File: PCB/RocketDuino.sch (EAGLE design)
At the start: 42 parts, among them J1 FTDI, Y1 16MHZ

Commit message: New DRU settings
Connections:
- net RX2: now also SERIAL2.2; no longer SERIAL2.3
- net TX2: now also SERIAL2.3; no longer SERIAL2.2
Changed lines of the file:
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@@
 </segment>
 <segment>
-<pinref part="SERIAL2" gate="G$1" pin="2"/>
-<wire x1="256.54" y1="185.42" x2="264.16" y2="185.42" width="0.1524" layer="91"/>
-<label x="259.08" y="185.42" size="1.778" layer="95"/>
+<pinref part="SERIAL2" gate="G$1" pin="3"/>
+<wire x1="256.54" y1="187.96" x2="264.16" y2="187.96" width="0.1524" layer="91"/>
+<label x="259.08" y="187.96" size="1.778" layer="95"/>
 </segment>
 </net>
@@
 </segment>
 <segment>
-<pinref part="SERIAL2" gate="G$1" pin="3"/>
-<wire x1="256.54" y1="187.96" x2="264.16" y2="187.96" width="0.1524" layer="91"/>
-<label x="259.08" y="187.96" size="1.778" layer="95"/>
+<pinref part="SERIAL2" gate="G$1" pin="2"/>
+<wire x1="256.54" y1="185.42" x2="264.16" y2="185.42" width="0.1524" layer="91"/>
+<label x="259.08" y="185.42" size="1.778" layer="95"/>
 </segment>
 </net>

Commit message: Cleanups from Reddit post
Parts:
- added C11, C12: 0.1uF, SparkFun-Capacitors:CAP1206
- R1, R3: value 100Ω -> 150Ω
- R2, R4: value 150Ω -> 220Ω
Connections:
- net 5V: now also C11.1, C12.1
- net GND: now also C11.2, C12.2
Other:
- note added: "0.8"
- note removed: "0.4"
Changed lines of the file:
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@@
 <part name="C8" library="SparkFun-Capacitors" deviceset="CAP" device="1206" value="0.1uF"/>
 <part name="C9" library="SparkFun-Capacitors" deviceset="CAP" device="1206" value="0.22uF"/>
-<part name="R4" library="SparkFun-Resistors" deviceset="RESISTOR" device="1206" value="150Ω"/>
+<part name="R4" library="SparkFun-Resistors" deviceset="RESISTOR" device="1206" value="220Ω"/>
 <part name="R10" library="SparkFun-Resistors" deviceset="RESISTOR" device="1206" value="10KΩ"/>
 <part name="GND7" library="SparkFun-Aesthetics" deviceset="GND" device=""/>
@@
 <part name="GND13" library="SparkFun-Aesthetics" deviceset="GND" device=""/>
 <part name="POWER" library="led" deviceset="LED" device="SML0805"/>
-<part name="R1" library="SparkFun-Resistors" deviceset="RESISTOR" device="1206" value="100Ω"/>
+<part name="R1" library="SparkFun-Resistors" deviceset="RESISTOR" device="1206" value="150Ω"/>
 <part name="GPS" library="led" deviceset="LED" device="SML0805"/>
-<part name="R3" library="SparkFun-Resistors" deviceset="RESISTOR" device="1206" value="100Ω"/>
+<part name="R3" library="SparkFun-Resistors" deviceset="RESISTOR" device="1206" value="150Ω"/>
 <part name="RX" library="led" deviceset="LED" device="SML0805"/>
-<part name="R2" library="SparkFun-Resistors" deviceset="RESISTOR" device="1206" value="150Ω"/>
+<part name="R2" library="SparkFun-Resistors" deviceset="RESISTOR" device="1206" value="220Ω"/>
 <part name="MOS1" library="SparkFun-DiscreteSemi" deviceset="MOSFET-NCHANNEL" device="FQP30N06L" value=""/>
 <part name="MOS2" library="SparkFun-DiscreteSemi" deviceset="MOSFET-NCHANNEL" device="FQP30N06L" value=""/>
@@
 <part name="SERIAL2" library="SparkFun-Connectors" deviceset="M04" device="POLAR"/>
 <part name="SUPPLY6" library="SparkFun-Aesthetics" deviceset="5V" device=""/>
+<part name="C11" library="SparkFun-Capacitors" deviceset="CAP" device="1206" value="0.1uF"/>
+<part name="C12" library="SparkFun-Capacitors" deviceset="CAP" device="1206" value="0.1uF"/>
 </parts>
 <sheets>
@@
 <text x="147.32" y="40.64" size="1.778" layer="97">red</text>
 <text x="231.14" y="2.54" size="5.08" layer="97">Joshua Villwock</text>
-<text x="299.974" y="1.27" size="3.81" layer="97">0.4</text>
+<text x="299.974" y="1.27" size="3.81" layer="97">0.8</text>
 <wire x1="-5.08" y1="266.7" x2="312.42" y2="266.7" width="0.1524" layer="94"/>
 <wire x1="312.42" y1="266.7" x2="312.42" y2="-5.08" width="0.1524" layer="94"/>
@@
 <instance part="SERIAL2" gate="G$1" x="251.46" y="185.42"/>
 <instance part="SUPPLY6" gate="G$1" x="259.08" y="190.5"/>
+<instance part="C11" gate="G$1" x="48.26" y="180.34"/>
+<instance part="C12" gate="G$1" x="38.1" y="180.34"/>
 </instances>
 <busses>
@@
 <wire x1="58.42" y1="177.8" x2="58.42" y2="172.72" width="0.1524" layer="91"/>
 <wire x1="58.42" y1="172.72" x2="71.12" y2="172.72" width="0.1524" layer="91"/>
+<pinref part="C12" gate="G$1" pin="2"/>
+<wire x1="58.42" y1="172.72" x2="48.26" y2="172.72" width="0.1524" layer="91"/>
+<wire x1="48.26" y1="172.72" x2="38.1" y2="172.72" width="0.1524" layer="91"/>
+<wire x1="38.1" y1="172.72" x2="38.1" y2="177.8" width="0.1524" layer="91"/>
+<junction x="58.42" y="172.72"/>
+<pinref part="C11" gate="G$1" pin="2"/>
+<wire x1="48.26" y1="177.8" x2="48.26" y2="172.72" width="0.1524" layer="91"/>
+<junction x="48.26" y="172.72"/>
 </segment>
 <segment>
@@
 <wire x1="58.42" y1="185.42" x2="58.42" y2="190.5" width="0.1524" layer="91"/>
 <wire x1="58.42" y1="190.5" x2="68.58" y2="190.5" width="0.1524" layer="91"/>
+<pinref part="C12" gate="G$1" pin="1"/>
+<wire x1="58.42" y1="190.5" x2="48.26" y2="190.5" width="0.1524" layer="91"/>
+<wire x1="48.26" y1="190.5" x2="38.1" y2="190.5" width="0.1524" layer="91"/>
+<wire x1="38.1" y1="190.5" x2="38.1" y2="185.42" width="0.1524" layer="91"/>
+<junction x="58.42" y="190.5"/>
+<pinref part="C11" gate="G$1" pin="1"/>
+<wire x1="48.26" y1="185.42" x2="48.26" y2="190.5" width="0.1524" layer="91"/>
+<junction x="48.26" y="190.5"/>
 </segment>
 <segment>
@@
 </sheet>
 </sheets>
-<errors>
-</errors>
 </schematic>
 </drawing>

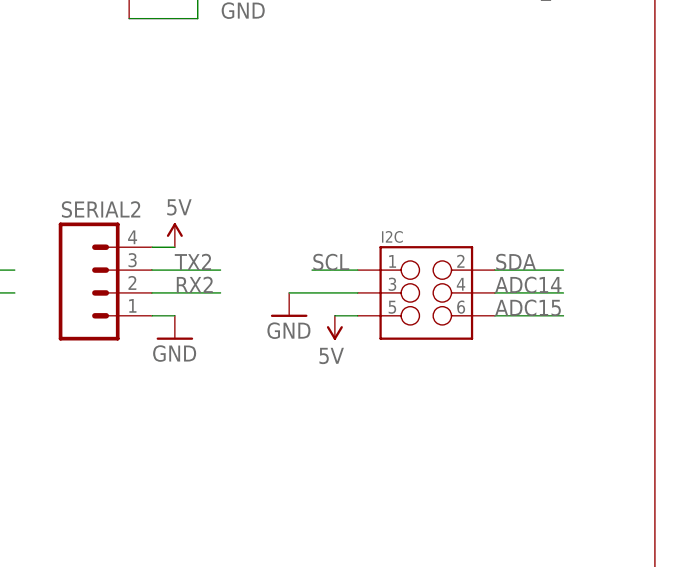
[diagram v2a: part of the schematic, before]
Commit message: Non-SMT I2C connector
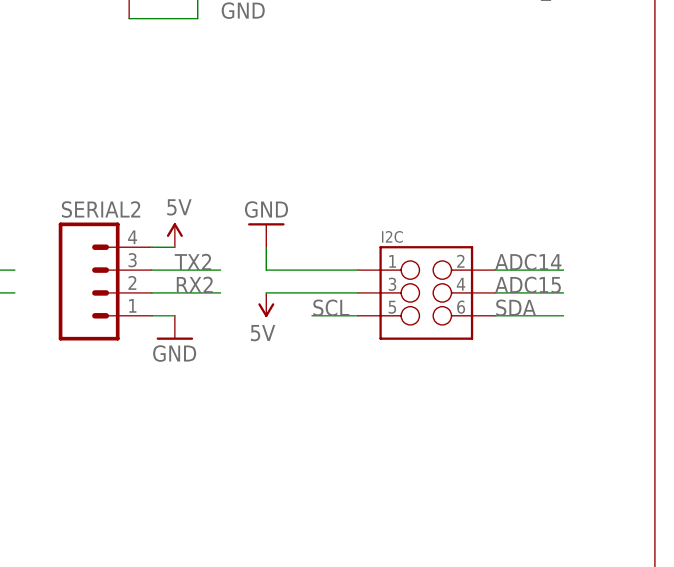
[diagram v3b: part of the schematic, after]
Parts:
- I2C: device SparkFun-Connectors:M03X2FEMALE_SMD -> SparkFun-Connectors:M03X2FEMALE
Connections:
- net 5V: now also I2C.3; no longer I2C.5
- net ADC14: now also I2C.2; no longer I2C.4
- net ADC15: now also I2C.4; no longer I2C.6
- net GND: now also I2C.1; no longer I2C.3
- net SCL: now also I2C.5; no longer I2C.1
- net SDA: now also I2C.6; no longer I2C.2
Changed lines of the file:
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@@
 <part name="GND8" library="SparkFun-Aesthetics" deviceset="GND" device=""/>
 <part name="SUPPLY4" library="SparkFun-Aesthetics" deviceset="5V" device=""/>
-<part name="I2C" library="SparkFun-Connectors" deviceset="M03X2" device="FEMALE_SMD"/>
-<part name="SUPPLY10" library="SparkFun-Aesthetics" deviceset="5V" device=""/>
-<part name="GND14" library="SparkFun-Aesthetics" deviceset="GND" device=""/>
+<part name="I2C" library="SparkFun-Connectors" deviceset="M03X2" device="FEMALE"/>
 <part name="FRAME1" library="SparkFun-Aesthetics" deviceset="FRAME-LEDGER" device=""/>
 <part name="GND15" library="SparkFun-Aesthetics" deviceset="GND" device=""/>
@@
 <part name="C11" library="SparkFun-Capacitors" deviceset="CAP" device="1206" value="0.1uF"/>
 <part name="C12" library="SparkFun-Capacitors" deviceset="CAP" device="1206" value="0.1uF"/>
+<part name="SUPPLY7" library="SparkFun-Aesthetics" deviceset="5V" device=""/>
+<part name="GND10" library="SparkFun-Aesthetics" deviceset="GND" device=""/>
 </parts>
 <sheets>
@@
 <instance part="SUPPLY4" gate="G$1" x="287.02" y="83.82"/>
 <instance part="I2C" gate="G$1" x="287.02" y="185.42"/>
-<instance part="SUPPLY10" gate="G$1" x="276.86" y="182.88" rot="R180"/>
-<instance part="GND14" gate="1" x="271.78" y="182.88"/>
 <instance part="FRAME1" gate="G$2" x="210.82" y="-5.08"/>
 <instance part="GND15" gate="1" x="289.56" y="251.46"/>
@@
 <instance part="C11" gate="G$1" x="48.26" y="180.34"/>
 <instance part="C12" gate="G$1" x="38.1" y="180.34"/>
+<instance part="SUPPLY7" gate="G$1" x="269.24" y="185.42" rot="R180"/>
+<instance part="GND10" gate="1" x="269.24" y="193.04" rot="R180"/>
 </instances>
 <busses>
@@
 </segment>
 <segment>
-<pinref part="GND14" gate="1" pin="GND"/>
-<pinref part="I2C" gate="G$1" pin="3"/>
-<wire x1="271.78" y1="185.42" x2="279.4" y2="185.42" width="0.1524" layer="91"/>
-</segment>
-<segment>
 <pinref part="MOS" gate="G$1" pin="2"/>
 <pinref part="GND15" gate="1" pin="GND"/>
@@
 <wire x1="228.6" y1="182.88" x2="231.14" y2="182.88" width="0.1524" layer="91"/>
 <pinref part="GND16" gate="1" pin="GND"/>
+</segment>
+<segment>
+<pinref part="GND10" gate="1" pin="GND"/>
+<wire x1="269.24" y1="190.5" x2="269.24" y2="187.96" width="0.1524" layer="91"/>
+<pinref part="I2C" gate="G$1" pin="1"/>
+<wire x1="269.24" y1="187.96" x2="279.4" y2="187.96" width="0.1524" layer="91"/>
 </segment>
 </net>
@@
 </segment>
 <segment>
-<pinref part="SUPPLY10" gate="G$1" pin="5V"/>
-<pinref part="I2C" gate="G$1" pin="5"/>
-<wire x1="276.86" y1="182.88" x2="279.4" y2="182.88" width="0.1524" layer="91"/>
-</segment>
-<segment>
 <pinref part="SERIAL1" gate="G$1" pin="4"/>
 <wire x1="228.6" y1="190.5" x2="231.14" y2="190.5" width="0.1524" layer="91"/>
@@
 <pinref part="SUPPLY6" gate="G$1" pin="5V"/>
 <wire x1="256.54" y1="190.5" x2="259.08" y2="190.5" width="0.1524" layer="91"/>
+</segment>
+<segment>
+<pinref part="SUPPLY7" gate="G$1" pin="5V"/>
+<pinref part="I2C" gate="G$1" pin="3"/>
+<wire x1="269.24" y1="185.42" x2="279.4" y2="185.42" width="0.1524" layer="91"/>
 </segment>
 </net>
@@
 </segment>
 <segment>
+<pinref part="I2C" gate="G$1" pin="6"/>
+<wire x1="294.64" y1="182.88" x2="302.26" y2="182.88" width="0.1524" layer="91"/>
+<label x="294.64" y="182.88" size="1.778" layer="95"/>
+</segment>
+</net>
+<net name="SCL" class="0">
+<segment>
+<pinref part="ATMEGA2560AU" gate="1" pin="(SCL/INT0)PD0"/>
+<wire x1="160.02" y1="132.08" x2="149.86" y2="132.08" width="0.1524" layer="91"/>
+<label x="152.4" y="132.08" size="1.778" layer="95"/>
+</segment>
+<segment>
+<pinref part="I2C" gate="G$1" pin="5"/>
+<wire x1="279.4" y1="182.88" x2="274.32" y2="182.88" width="0.1524" layer="91"/>
+<label x="274.32" y="182.88" size="1.778" layer="95"/>
+</segment>
+</net>
+<net name="ADC14" class="0">
+<segment>
+<pinref part="ATMEGA2560AU" gate="1" pin="PK6(ADC14/PCINT22)"/>
+<wire x1="78.74" y1="129.54" x2="68.58" y2="129.54" width="0.1524" layer="91"/>
+<label x="68.58" y="129.54" size="1.778" layer="95"/>
+</segment>
+<segment>
 <pinref part="I2C" gate="G$1" pin="2"/>
 <wire x1="294.64" y1="187.96" x2="302.26" y2="187.96" width="0.1524" layer="91"/>
@@
 </segment>
 </net>
-<net name="SCL" class="0">
-<segment>
-<pinref part="ATMEGA2560AU" gate="1" pin="(SCL/INT0)PD0"/>
-<wire x1="160.02" y1="132.08" x2="149.86" y2="132.08" width="0.1524" layer="91"/>
-<label x="152.4" y="132.08" size="1.778" layer="95"/>
-</segment>
-<segment>
-<pinref part="I2C" gate="G$1" pin="1"/>
-<wire x1="279.4" y1="187.96" x2="274.32" y2="187.96" width="0.1524" layer="91"/>
-<label x="274.32" y="187.96" size="1.778" layer="95"/>
-</segment>
-</net>
-<net name="ADC14" class="0">
-<segment>
-<pinref part="ATMEGA2560AU" gate="1" pin="PK6(ADC14/PCINT22)"/>
-<wire x1="78.74" y1="129.54" x2="68.58" y2="129.54" width="0.1524" layer="91"/>
-<label x="68.58" y="129.54" size="1.778" layer="95"/>
+<net name="ADC15" class="0">
+<segment>
+<pinref part="ATMEGA2560AU" gate="1" pin="PK7(ADC15/PCINT23)"/>
+<wire x1="78.74" y1="132.08" x2="68.58" y2="132.08" width="0.1524" layer="91"/>
+<label x="68.58" y="132.08" size="1.778" layer="95"/>
 </segment>
 <segment>
@@
 </segment>
 </net>
-<net name="ADC15" class="0">
-<segment>
-<pinref part="ATMEGA2560AU" gate="1" pin="PK7(ADC15/PCINT23)"/>
-<wire x1="78.74" y1="132.08" x2="68.58" y2="132.08" width="0.1524" layer="91"/>
-<label x="68.58" y="132.08" size="1.778" layer="95"/>
-</segment>
-<segment>
-<pinref part="I2C" gate="G$1" pin="6"/>
-<wire x1="294.64" y1="182.88" x2="302.26" y2="182.88" width="0.1524" layer="91"/>
-<label x="294.64" y="182.88" size="1.778" layer="95"/>
-</segment>
-</net>

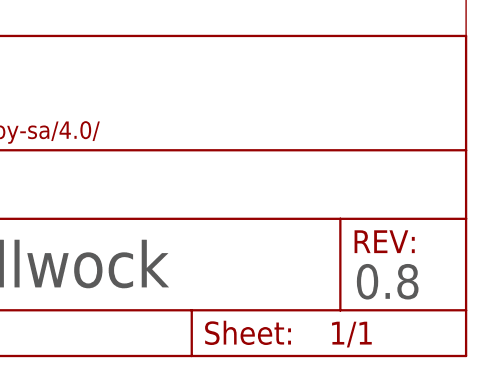
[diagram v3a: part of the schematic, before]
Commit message: Silkscreen Changes
Also re-routed the Vsense wire
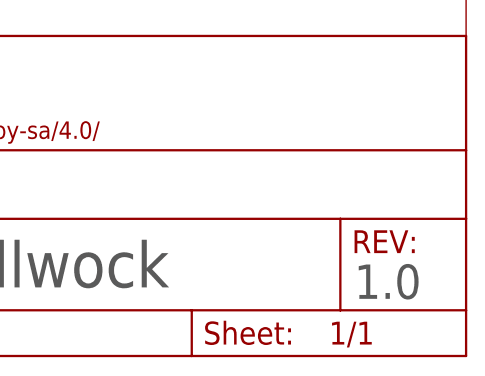
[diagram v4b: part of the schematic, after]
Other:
- note added: "1.0"
- note added: "RocketDuino"
- note removed: "0.8"
- note removed: "RocketDuino v0.4"
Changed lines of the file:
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@@
 <text x="147.32" y="40.64" size="1.778" layer="97">red</text>
 <text x="231.14" y="2.54" size="5.08" layer="97">Joshua Villwock</text>
-<text x="299.974" y="1.27" size="3.81" layer="97">0.8</text>
+<text x="299.974" y="1.27" size="3.81" layer="97">1.0</text>
 <wire x1="-5.08" y1="266.7" x2="312.42" y2="266.7" width="0.1524" layer="94"/>
 <wire x1="312.42" y1="266.7" x2="312.42" y2="-5.08" width="0.1524" layer="94"/>
 <wire x1="312.42" y1="-5.08" x2="-5.08" y2="-5.08" width="0.1524" layer="94"/>
 <wire x1="-5.08" y1="-5.08" x2="-5.08" y2="266.7" width="0.1524" layer="94"/>
-<text x="0" y="256.54" size="6.4516" layer="152">RocketDuino v0.4</text>
+<text x="0" y="256.54" size="6.4516" layer="152">RocketDuino</text>
 <wire x1="210.82" y1="106.68" x2="248.92" y2="106.68" width="0.1524" layer="105"/>
 <wire x1="210.82" y1="40.64" x2="248.92" y2="40.64" width="0.1524" layer="105"/>
@@
 </sheet>
 </sheets>
+<errors>
+</errors>
 </schematic>
 </drawing>
